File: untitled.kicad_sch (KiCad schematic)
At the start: 12 parts, among them U1 LM2596S-5, U2 LM2596S-12

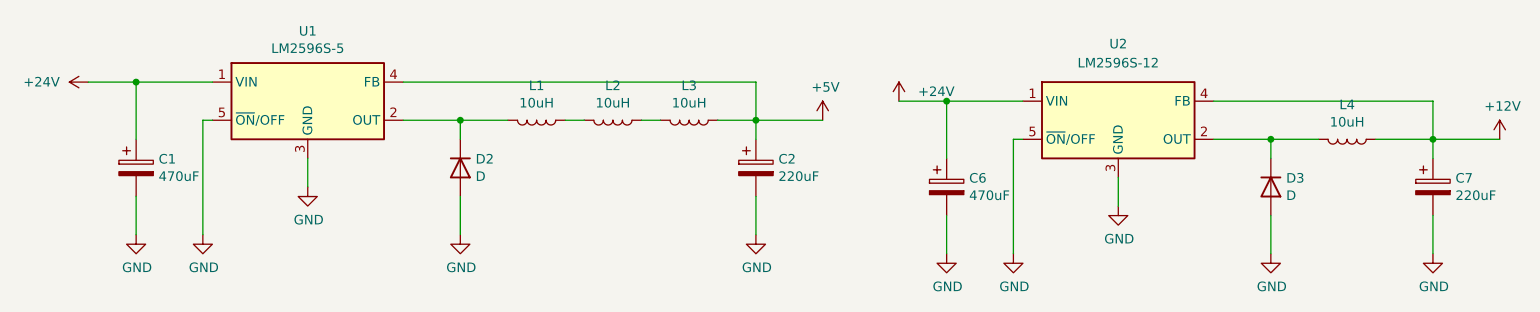
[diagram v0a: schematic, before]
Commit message: Create new design with LM2576
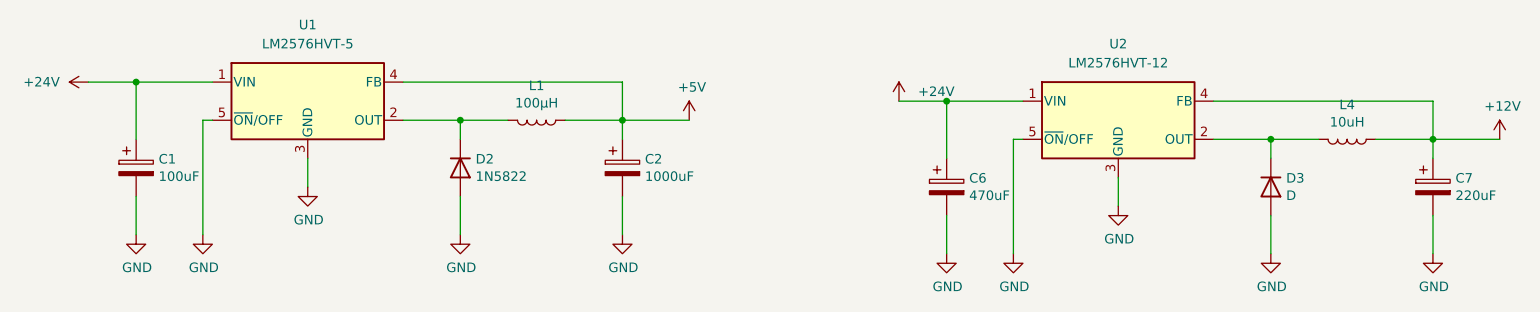
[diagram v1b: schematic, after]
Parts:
- removed L2, L3: 10uH, Inductor_SMD:L_TDK_SLF10145, symbol Device:L
- removed U1: LM2596S-5, Package_TO_SOT_SMD:TO-263-5_TabPin3, symbol Regulator_Switching:LM2596S-5
- removed U2: LM2596S-12, Package_TO_SOT_SMD:TO-263-5_TabPin3, symbol Regulator_Switching:LM2596S-12
- added U1: LM2576HVT-5, Package_TO_SOT_THT:TO-220-5_Vertical, symbol Regulator_Switching:LM2576HVT-5
- added U2: LM2576HVT-12, Package_TO_SOT_THT:TO-220-5_Vertical, symbol Regulator_Switching:LM2576HVT-12
- C1: value 470uF -> 100uF
- C2: value 220uF -> 1000uF
- D2: value D -> 1N5822
- L1: value 10uH -> 100µH
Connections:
- net +12V: now also U2.4 (FB)
- net +24V: now also U1.1 (VIN), U2.1 (VIN)
- net +5V: now also L1.1, U1.4 (FB)
- net GND: now also U1.3 (GND), U1.5 (~{ON}/OFF), U2.3 (GND), U2.5 (~{ON}/OFF)
- net at D2.1 (K), L1.2: now also U1.2 (OUT)
- net at D3.1 (K), L4.2: now also U2.2 (OUT)
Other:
- moved on the sheet: C2

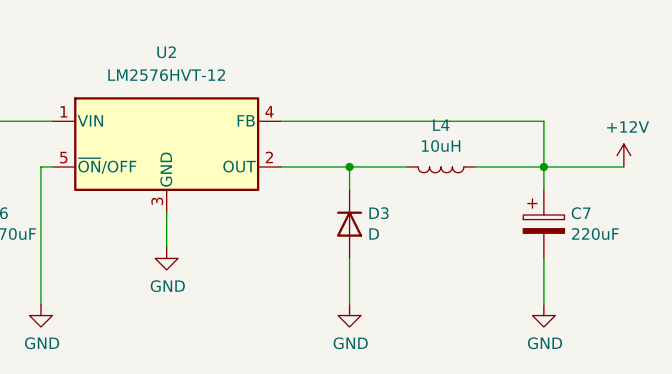
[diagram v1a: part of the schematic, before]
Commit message: replace LM2576 footprints
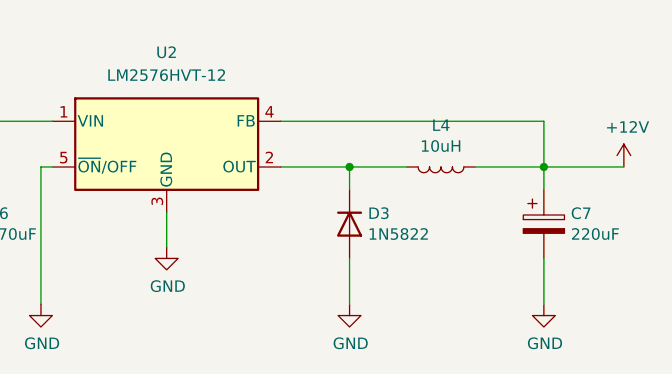
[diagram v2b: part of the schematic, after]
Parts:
- D3: value D -> 1N5822
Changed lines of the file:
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@@
     (pin "2")
+  )
+  (symbol (lib_id "Regulator_Switching:LM2576HVT-12") (at 186.69 46.99 0) (unit 1)
+    (in_bom yes) (on_board yes) (fields_autoplaced)
+    (property "Reference" "U2" (id 0) (at 186.69 36.83 0))
+    (property "Value" "LM2576HVT-12" (id 1) (at 186.69 39.37 0))
+    (property "Footprint" "Package_TO_SOT_THT:TO-220-5_Vertical" (id 2) (at 186.69 53.34 0)
+      (effects (font (size 1.27 1.27) italic) (justify left) hide)
+    )
+    (property "Datasheet" "http://www.ti.com/lit/ds/symlink/lm2576.pdf" (id 3) (at 186.69 46.99 0)
+      (effects (font (size 1.27 1.27)) hide)
+    )
+    (pin "1")
+    (pin "2")
+    (pin "3")
+    (pin "4")
+    (pin "5")
   )
   (symbol (lib_id "Device:L") (at 217.17 49.53 270) (unit 1)
@@
       (effects (font (size 1.27 1.27)) (justify left))
     )
-    (property "Value" "D" (id 1) (at 209.042 57.023 90)
+    (property "Value" "1N5822" (id 1) (at 209.042 57.023 90)
       (effects (font (size 1.27 1.27)) (justify left))
     )
@@
       (effects (font (size 1.27 1.27)) hide)
     )
-    (pin "1")
-    (pin "2")
-    (pin "3")
-    (pin "4")
-    (pin "5")
-  )
-  (symbol (lib_id "Regulator_Switching:LM2576HVT-12") (at 186.69 46.99 0) (unit 1)
-    (in_bom yes) (on_board yes) (fields_autoplaced)
-    (property "Reference" "U2" (id 0) (at 186.69 36.83 0))
-    (property "Value" "LM2576HVT-12" (id 1) (at 186.69 39.37 0))
-    (property "Footprint" "Package_TO_SOT_THT:TO-220-5_Vertical" (id 2) (at 186.69 53.34 0)
-      (effects (font (size 1.27 1.27) italic) (justify left) hide)
-    )
-    (property "Datasheet" "http://www.ti.com/lit/ds/symlink/lm2576.pdf" (id 3) (at 186.69 46.99 0)
-      (effects (font (size 1.27 1.27)) hide)
-    )

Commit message: Change discrete components
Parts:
- C1: value 100uF -> 100µF
- C6: value 470uF -> 100µF
- C7: value 220uF -> 1000µF
- L1: value 100µH -> 150µF
- L4: value 10uH -> 220µH
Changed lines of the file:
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@@
       (effects (font (size 1.27 1.27)) (justify left))
     )
-    (property "Value" "100uF" (id 1) (at 58.8772 54.483 0)
+    (property "Value" "100µF" (id 1) (at 58.8772 54.483 0)
       (effects (font (size 1.27 1.27)) (justify left))
     )
@@
       (effects (font (size 1.27 1.27)) (justify left))
     )
-    (property "Value" "470uF" (id 1) (at 166.8272 57.023 0)
+    (property "Value" "100µF" (id 1) (at 166.8272 57.023 0)
       (effects (font (size 1.27 1.27)) (justify left))
     )
@@
     (in_bom yes) (on_board yes)
     (property "Reference" "L4" (id 0) (at 217.17 44.9326 90))
-    (property "Value" "10uH" (id 1) (at 217.17 47.244 90))
+    (property "Value" "220µH" (id 1) (at 217.17 47.244 90))
     (property "Footprint" "Inductor_SMD:L_TDK_SLF10145" (id 2) (at 217.17 49.53 0)
       (effects (font (size 1.27 1.27)) hide)
@@
       (effects (font (size 1.27 1.27)) (justify left))
     )
-    (property "Value" "220uF" (id 1) (at 231.5972 57.023 0)
+    (property "Value" "1000µF" (id 1) (at 231.5972 57.023 0)
       (effects (font (size 1.27 1.27)) (justify left))
     )
@@
     (in_bom yes) (on_board yes)
     (property "Reference" "L1" (id 0) (at 109.22 42.3926 90))
-    (property "Value" "100µH" (id 1) (at 109.22 44.704 90))
+    (property "Value" "150µF" (id 1) (at 109.22 44.704 90))
     (property "Footprint" "Inductor_SMD:L_TDK_SLF10145" (id 2) (at 109.22 46.99 0)
       (effects (font (size 1.27 1.27)) hide)
